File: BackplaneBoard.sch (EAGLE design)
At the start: 1 part

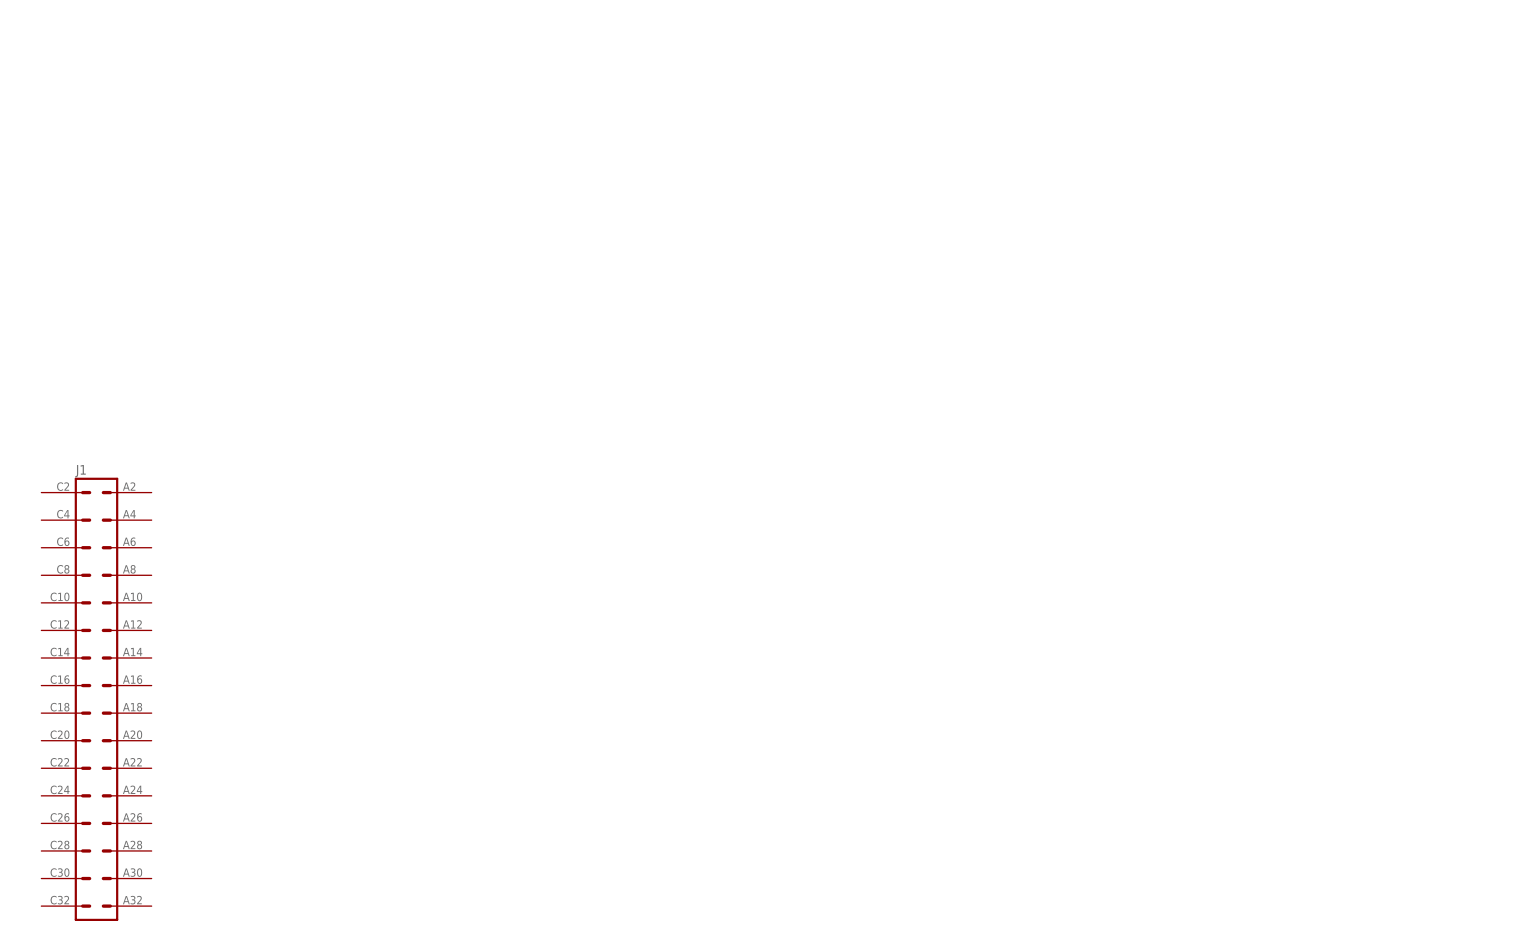
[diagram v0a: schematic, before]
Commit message: Added right connectors to board
added right connectors and put board size in, Melchor is slacking
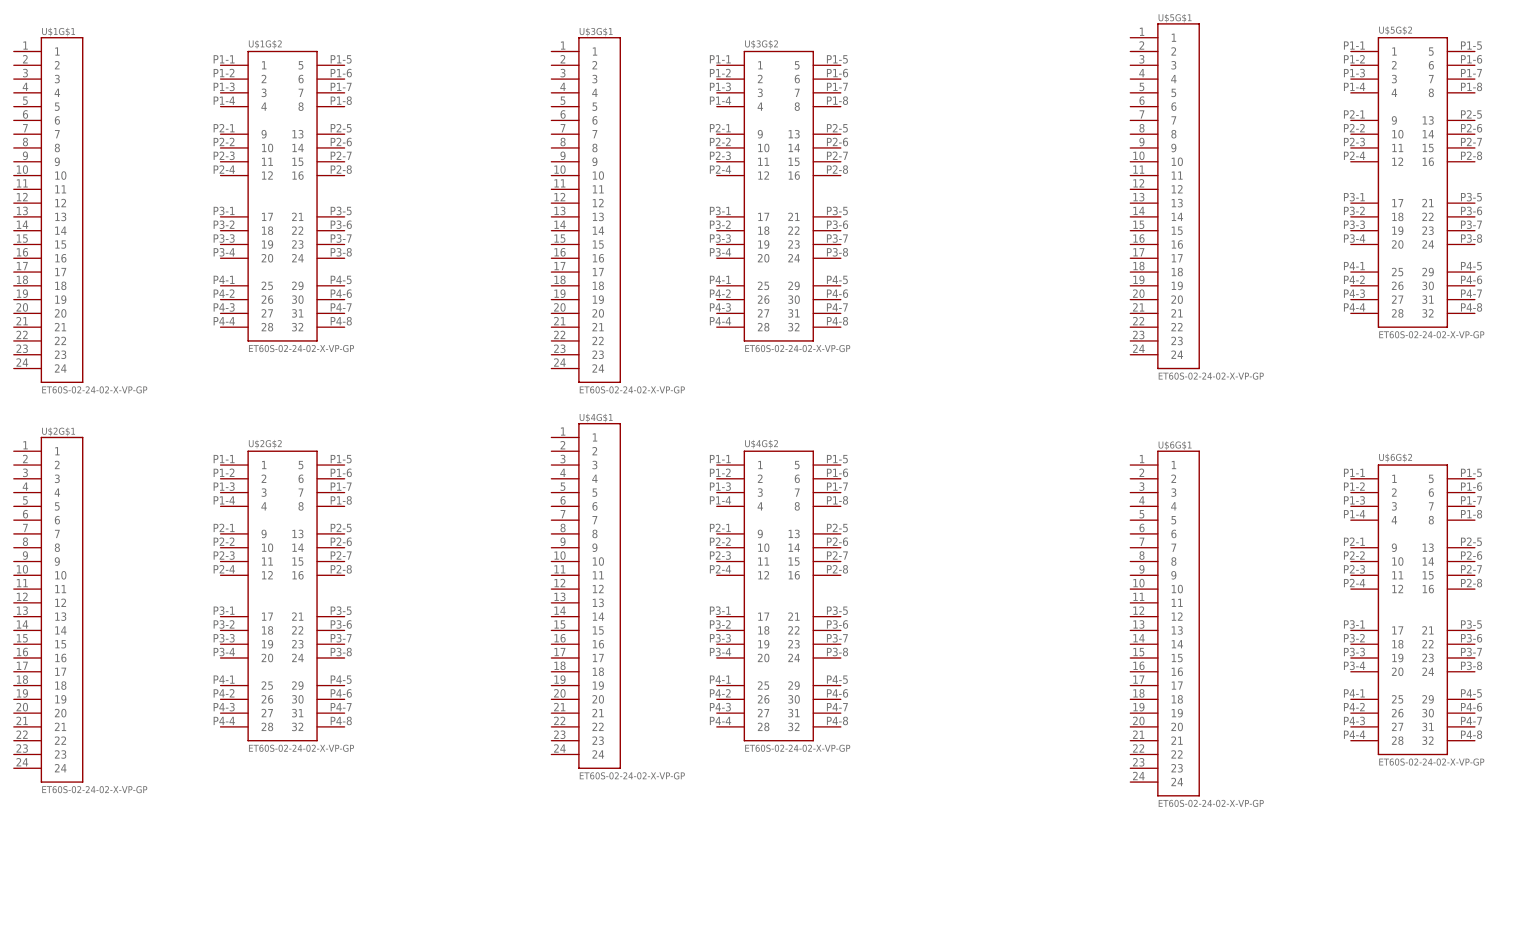
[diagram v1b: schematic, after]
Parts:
- removed J1: (no value), 19inch:VG32KB
- added U$1, U$2, U$3, U$4, U$5, U$6: ET60S-02-24-02-X-VP-GP, ET60S-02-24-02-X-VP-GP:ET60S-02-24-02-X-VP-GP
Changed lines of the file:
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@@
 <?xml version="1.0" encoding="utf-8"?>
 <!DOCTYPE eagle SYSTEM "eagle.dtd">
-<eagle version="9.3.0">
+<eagle version="9.2.0">
 <drawing>
 <settings>
@@
 </classes>
 <parts>
-<part name="J1" library="19inch" library_urn="urn:adsk.eagle:library:79" deviceset="VG32" device="KB" package3d_urn="urn:adsk.eagle:package:686/1"/>
+<part name="FRAME1" library="frames" library_urn="urn:adsk.eagle:library:229" deviceset="A4L-LOC" device=""/>
+<part name="U$1" library="ET60S-02-24-02-X-VP-GP" deviceset="ET60S-02-24-02-X-VP-GP" device=""/>
+<part name="U$2" library="ET60S-02-24-02-X-VP-GP" deviceset="ET60S-02-24-02-X-VP-GP" device=""/>
+<part name="U$3" library="ET60S-02-24-02-X-VP-GP" deviceset="ET60S-02-24-02-X-VP-GP" device=""/>
+<part name="U$4" library="ET60S-02-24-02-X-VP-GP" deviceset="ET60S-02-24-02-X-VP-GP" device=""/>
+<part name="U$5" library="ET60S-02-24-02-X-VP-GP" deviceset="ET60S-02-24-02-X-VP-GP" device=""/>
+<part name="U$6" library="ET60S-02-24-02-X-VP-GP" deviceset="ET60S-02-24-02-X-VP-GP" device=""/>
+<part name="FRAME2" library="frames" library_urn="urn:adsk.eagle:library:229" deviceset="A4L-LOC" device=""/>
 </parts>
 <sheets>
@@
 </plain>
 <instances>
-<instance part="J1" gate="G$1" x="99.06" y="38.1" smashed="yes">
-<attribute name="VALUE" x="95.25" y="-2.54" size="1.778" layer="96"/>
-<attribute name="NAME" x="95.25" y="82.042" size="1.778" layer="95"/>
+<instance part="FRAME1" gate="G$1" x="0" y="0">
+<attribute name="DRAWING_NAME" x="217.17" y="15.24" size="2.54" layer="94"/>
+<attribute name="LAST_DATE_TIME" x="217.17" y="10.16" size="2.286" layer="94"/>
+<attribute name="SHEET" x="230.505" y="5.08" size="2.54" layer="94"/>
+</instance>
+<instance part="U$1" gate="G$1" x="83.82" y="160.02">
+<attribute name="NAME" x="88.9" y="163.068" size="1.27" layer="95"/>
+<attribute name="VALUE" x="88.9" y="97.028" size="1.27" layer="96"/>
+</instance>
+<instance part="U$1" gate="G$2" x="121.92" y="157.48">
+<attribute name="NAME" x="127" y="160.782" size="1.27" layer="95"/>
+<attribute name="VALUE" x="127" y="104.648" size="1.27" layer="96"/>
+</instance>
+<instance part="U$2" gate="G$1" x="83.82" y="86.36">
+<attribute name="NAME" x="88.9" y="89.408" size="1.27" layer="95"/>
+<attribute name="VALUE" x="88.9" y="23.368" size="1.27" layer="96"/>
+</instance>
+<instance part="U$2" gate="G$2" x="121.92" y="83.82">
+<attribute name="NAME" x="127" y="87.122" size="1.27" layer="95"/>
+<attribute name="VALUE" x="127" y="30.988" size="1.27" layer="96"/>
+</instance>
+<instance part="U$3" gate="G$1" x="182.88" y="160.02">
+<attribute name="NAME" x="187.96" y="163.068" size="1.27" layer="95"/>
+<attribute name="VALUE" x="187.96" y="97.028" size="1.27" layer="96"/>
+</instance>
+<instance part="U$3" gate="G$2" x="213.36" y="157.48">
+<attribute name="NAME" x="218.44" y="160.782" size="1.27" layer="95"/>
+<attribute name="VALUE" x="218.44" y="104.648" size="1.27" layer="96"/>
+</instance>
+<instance part="U$4" gate="G$1" x="182.88" y="88.9">
+<attribute name="NAME" x="187.96" y="91.948" size="1.27" layer="95"/>
+<attribute name="VALUE" x="187.96" y="25.908" size="1.27" layer="96"/>
+</instance>
+<instance part="U$4" gate="G$2" x="213.36" y="83.82">
+<attribute name="NAME" x="218.44" y="87.122" size="1.27" layer="95"/>
+<attribute name="VALUE" x="218.44" y="30.988" size="1.27" layer="96"/>
+</instance>
+<instance part="U$5" gate="G$1" x="289.56" y="162.56">
+<attribute name="NAME" x="294.64" y="165.608" size="1.27" layer="95"/>
+<attribute name="VALUE" x="294.64" y="99.568" size="1.27" layer="96"/>
+</instance>
+<instance part="U$5" gate="G$2" x="330.2" y="160.02">
+<attribute name="NAME" x="335.28" y="163.322" size="1.27" layer="95"/>
+<attribute name="VALUE" x="335.28" y="107.188" size="1.27" layer="96"/>
+</instance>
+<instance part="U$6" gate="G$1" x="289.56" y="83.82">
+<attribute name="NAME" x="294.64" y="86.868" size="1.27" layer="95"/>
+<attribute name="VALUE" x="294.64" y="20.828" size="1.27" layer="96"/>
+</instance>
+<instance part="U$6" gate="G$2" x="330.2" y="81.28">
+<attribute name="NAME" x="335.28" y="84.582" size="1.27" layer="95"/>
+<attribute name="VALUE" x="335.28" y="28.448" size="1.27" layer="96"/>
+</instance>
+<instance part="FRAME2" gate="G$1" x="261.62" y="0">
+<attribute name="DRAWING_NAME" x="478.79" y="15.24" size="2.54" layer="94"/>
+<attribute name="LAST_DATE_TIME" x="478.79" y="10.16" size="2.286" layer="94"/>
+<attribute name="SHEET" x="492.125" y="5.08" size="2.54" layer="94"/>
 </instance>
 </instances>
@@
 will not be understood (or retained) with this version.
 </note>
-<note version="8.3" severity="warning">
-Since Version 8.3, EAGLE supports the association of 3D packages
-with devices in libraries, schematics, and board files. Those 3D
-packages will not be understood (or retained) with this version.
-</note>
 </compatibility>

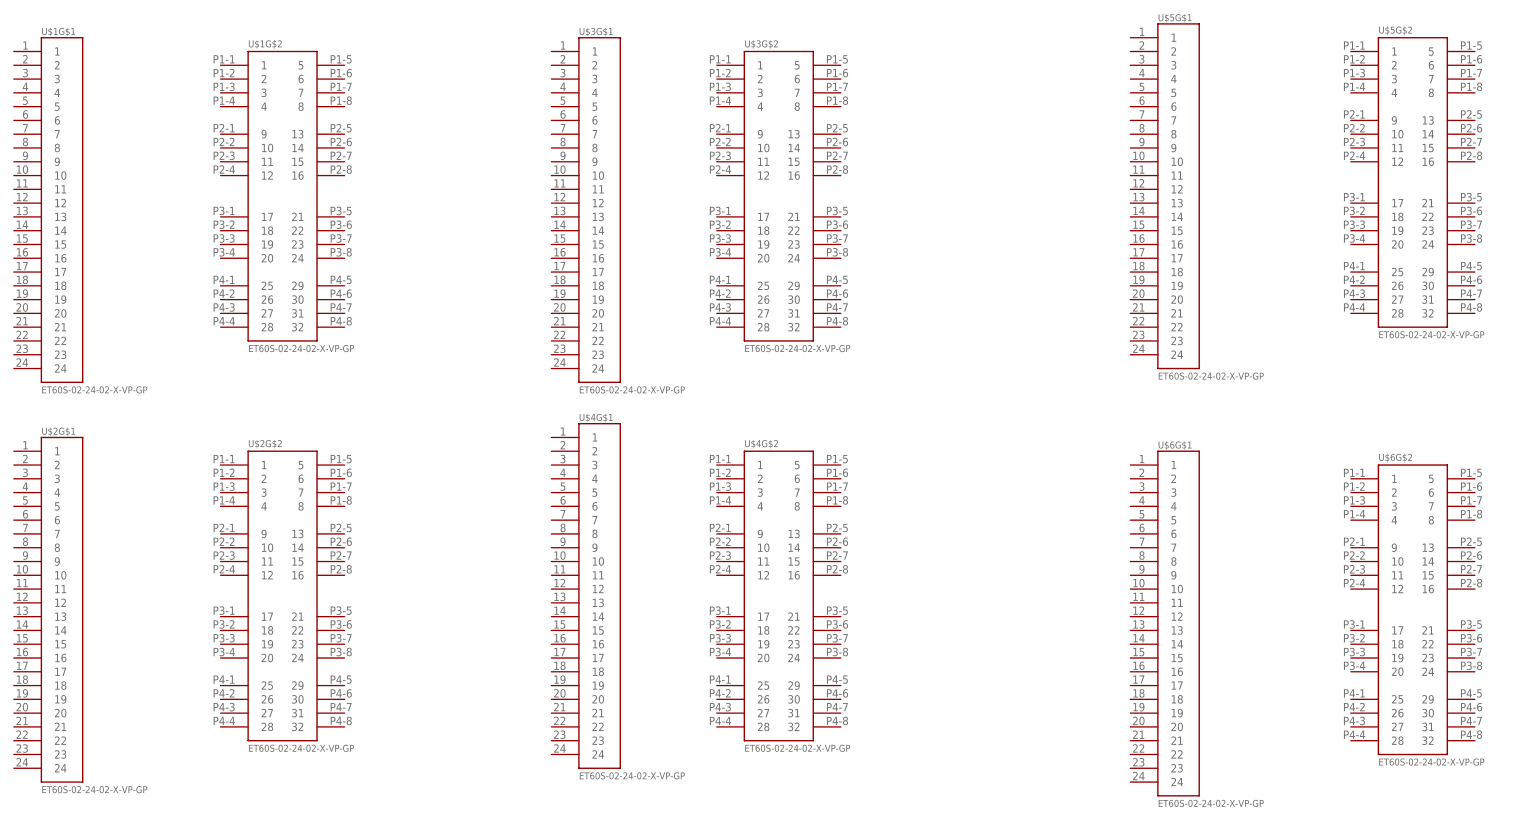
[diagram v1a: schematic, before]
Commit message: updated connectors
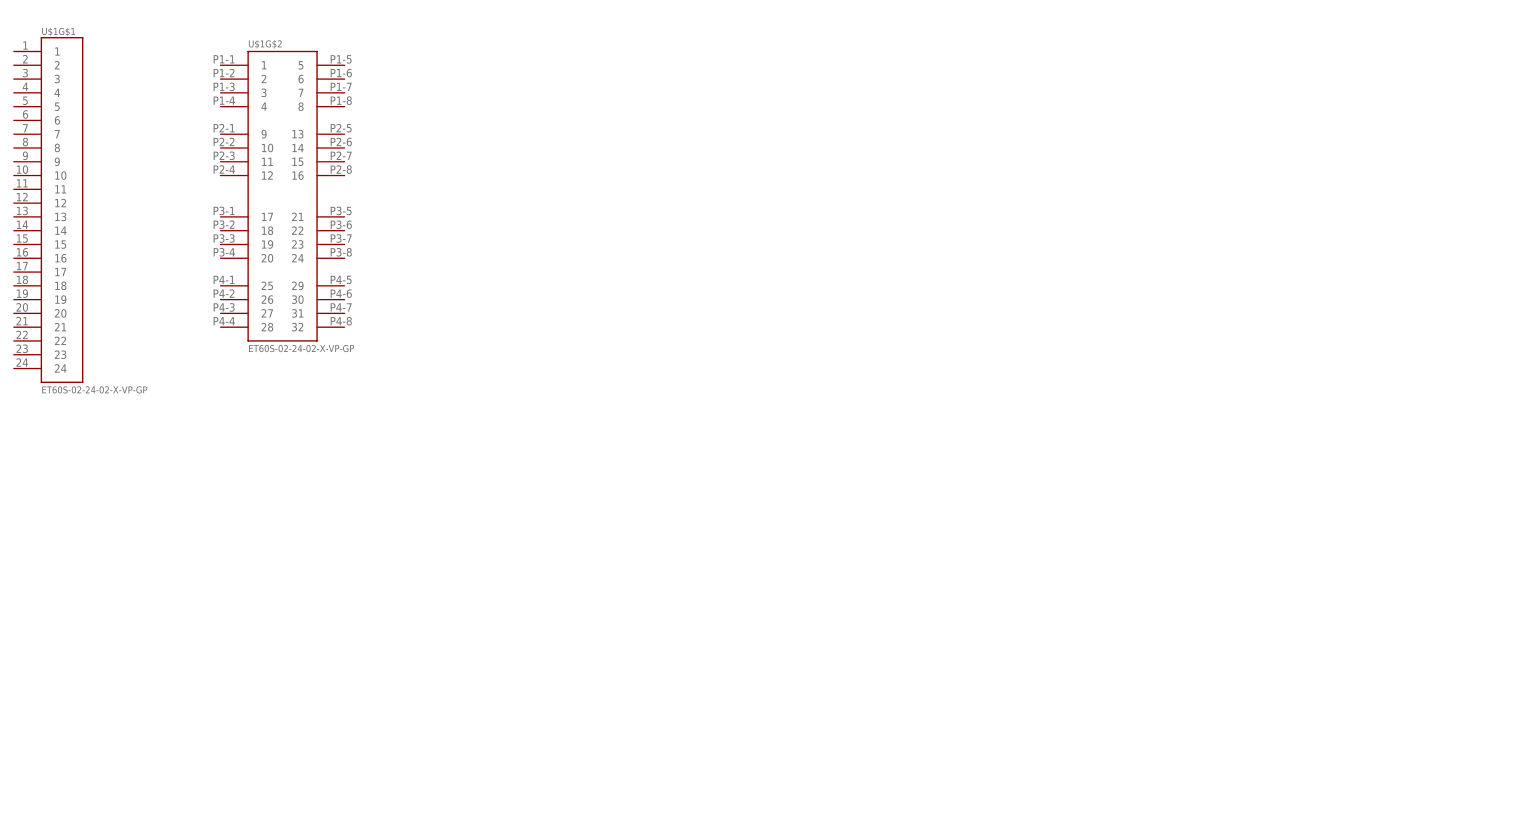
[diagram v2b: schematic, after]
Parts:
- removed U$2, U$3, U$4, U$5, U$6: ET60S-02-24-02-X-VP-GP, ET60S-02-24-02-X-VP-GP:ET60S-02-24-02-X-VP-GP
